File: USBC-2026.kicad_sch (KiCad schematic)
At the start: 28 parts, among them IC1 TPS25752ASRSMR, J1 USB_C_Receptacle, Q1 NMOS_Substrate, Q2 NMOS_Substrate, U1 TPS55288RPMR, U2 AT24C512C-SHM-B

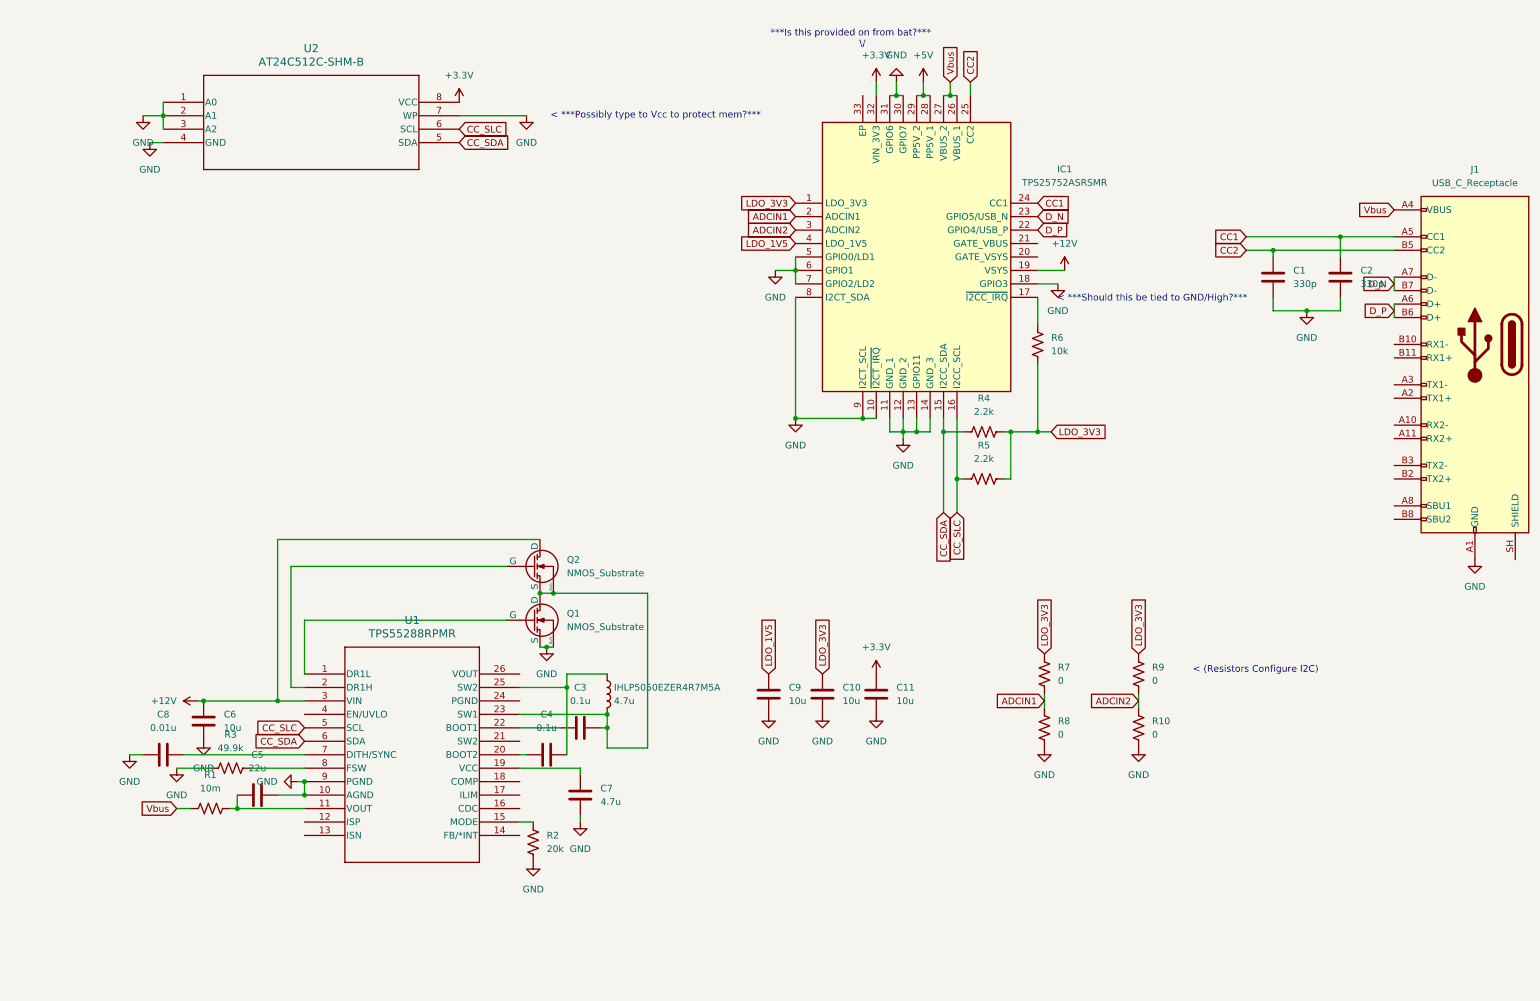
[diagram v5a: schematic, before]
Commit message: Grounded pins to select I2C address index 2.
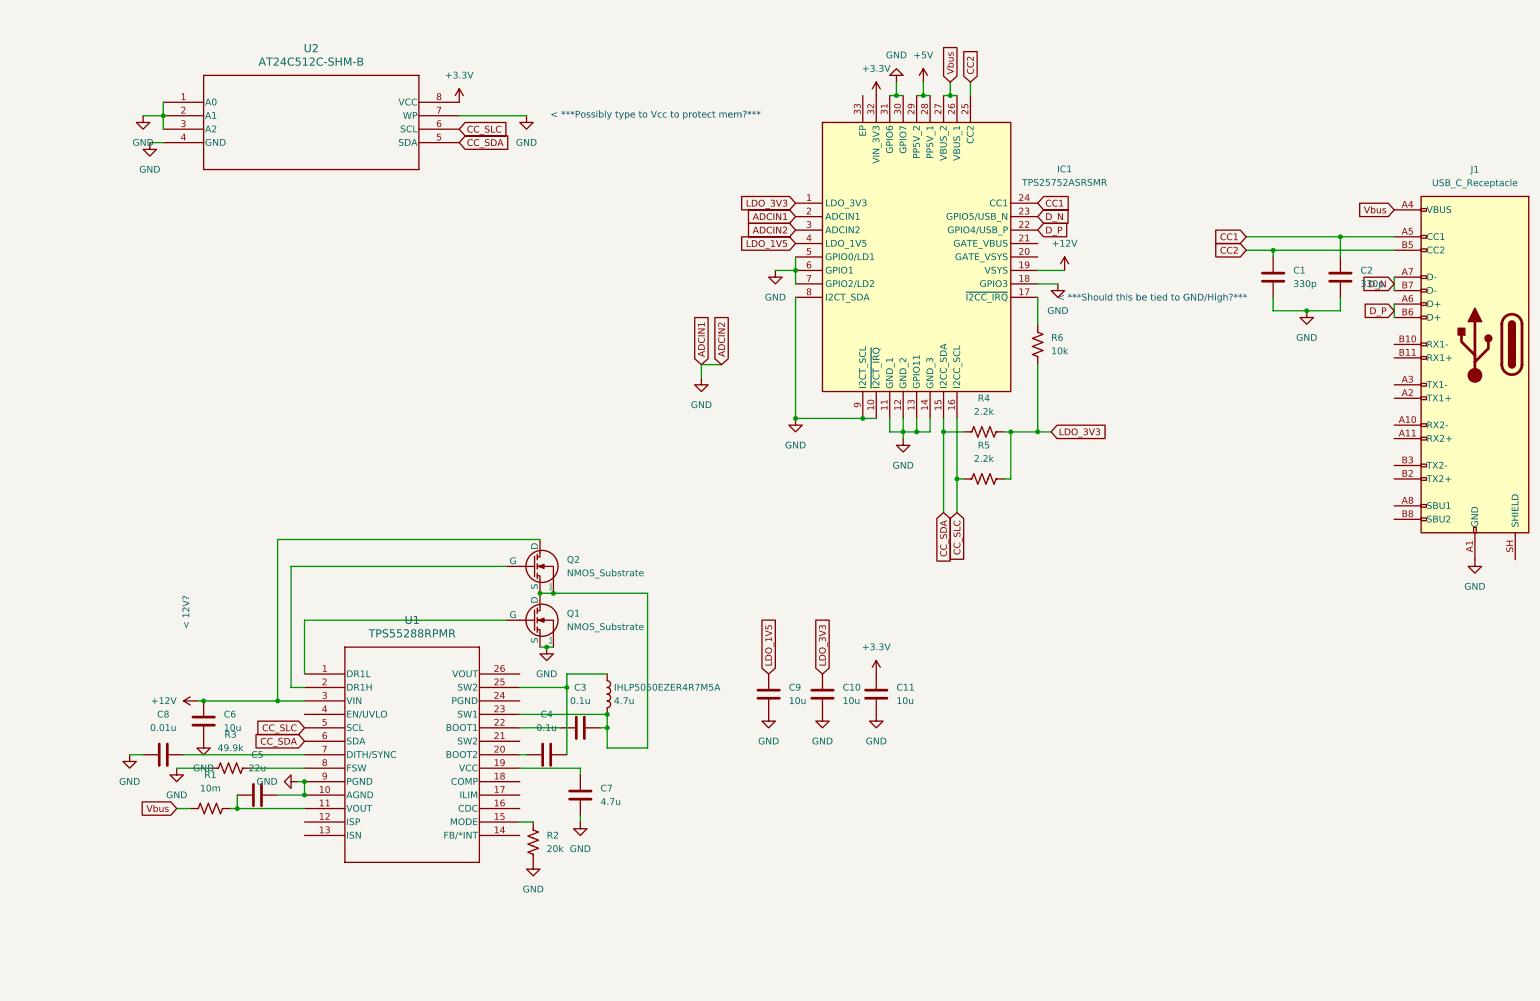
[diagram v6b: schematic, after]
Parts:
- removed R10, R7, R8, R9: 0, symbol Device:R_US
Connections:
- net ADCIN1 is gone; now on net GND: IC1.2 (ADCIN1)
- net ADCIN2 is gone; now on net GND: IC1.3 (ADCIN2)
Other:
- note added: "< 12V?"
- note removed: "***Is this provided on from bat?*** \/"
- note removed: "< (Resistors Configure I2C)"

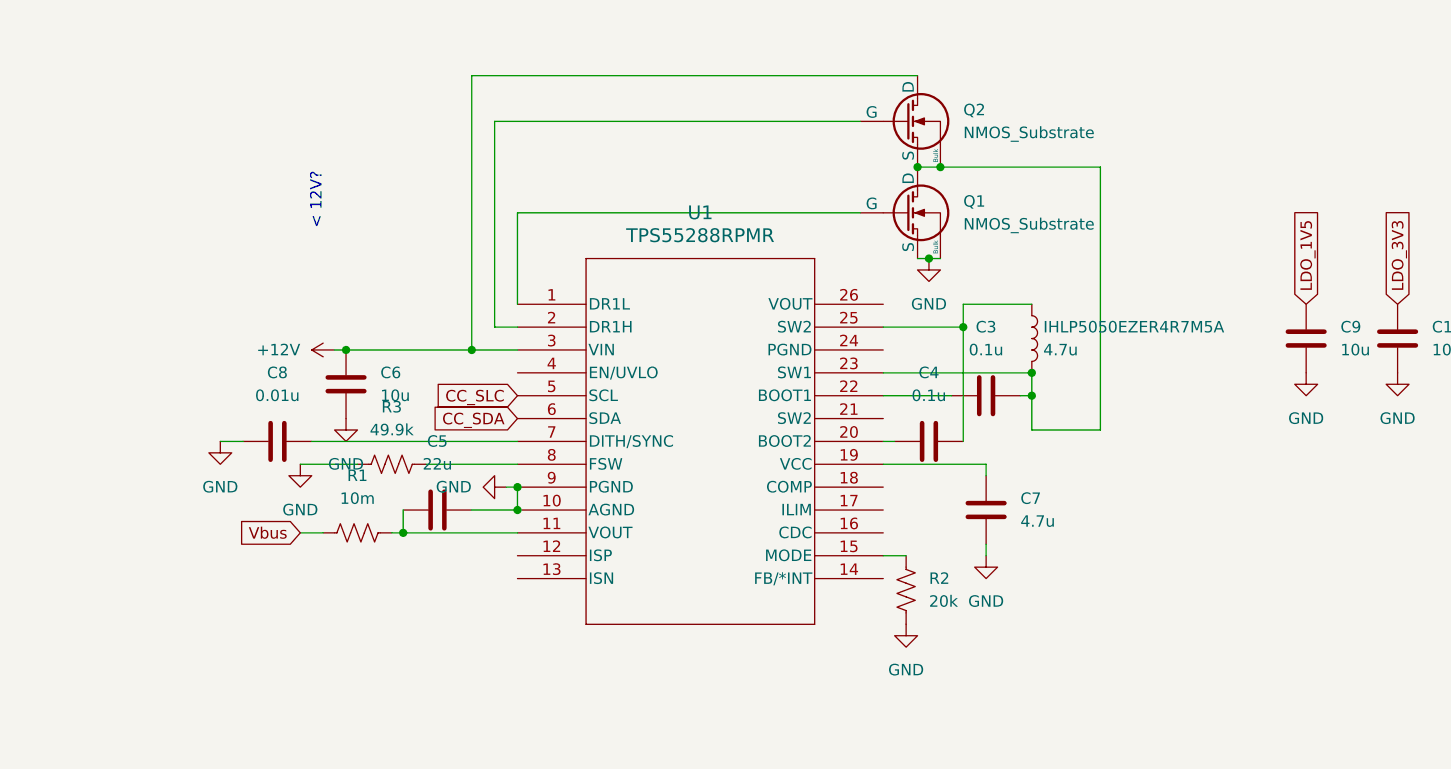
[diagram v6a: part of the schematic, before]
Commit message: Calculated and implemented loop stability components.
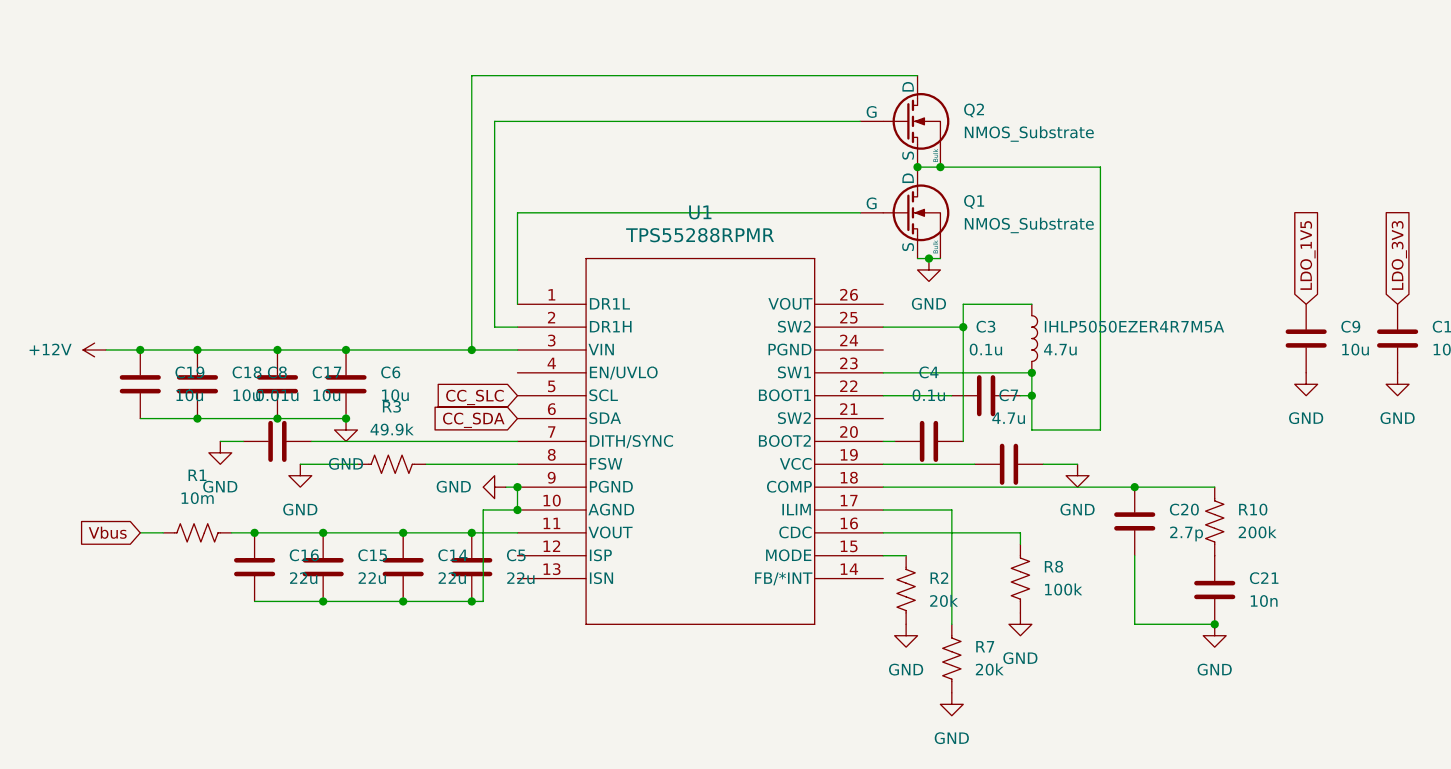
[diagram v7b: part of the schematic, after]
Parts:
- added C14, C15, C16: 22u, symbol Device:C
- added C17, C18, C19: 10u, symbol Device:C
- added C20: 2.7p, symbol Device:C
- added C21: 10n, symbol Device:C
- added R10: 200k, symbol Device:R_US
- added R7: 20k, symbol Device:R_US
- added R8: 100k, symbol Device:R_US
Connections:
- net +12V: now also C17.1, C18.1, C19.1
- net GND: now also C5.2, C7.2, C14.2, C15.2, C16.2, C17.2, C18.2, C19.2, C20.1, C21.1, R7.1, R8.1; no longer C5.1, C7.1
- net at R1.2, U1.11 (VOUT): now also C5.1, C14.1, C15.1, C16.1; no longer C5.2
- net at U1.19 (VCC): now also C7.1; no longer C7.2
- net at U1.16 (CDC): now also R8.2
- net at U1.17 (ILIM): now also R7.2
- net at U1.18 (COMP): now also C20.2, R10.2
- new net: C21.2, R10.1
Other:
- note removed: "< 12V?"
- moved on the sheet: C7, R1

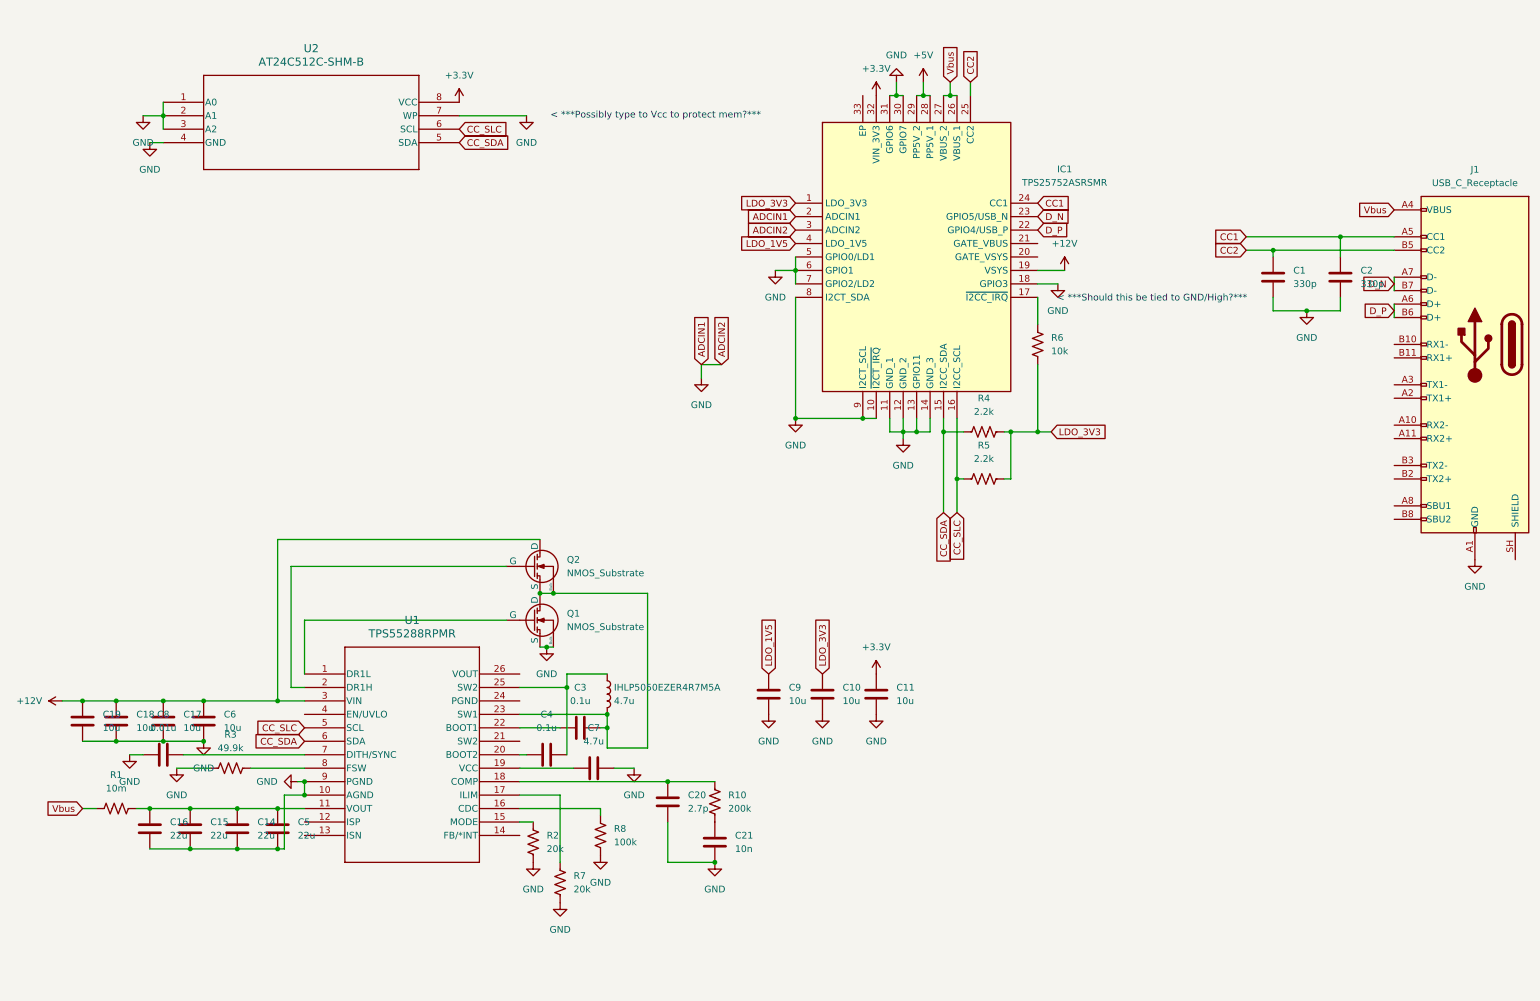
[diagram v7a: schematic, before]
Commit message: Added specific NMOS IC and split into subsheets.
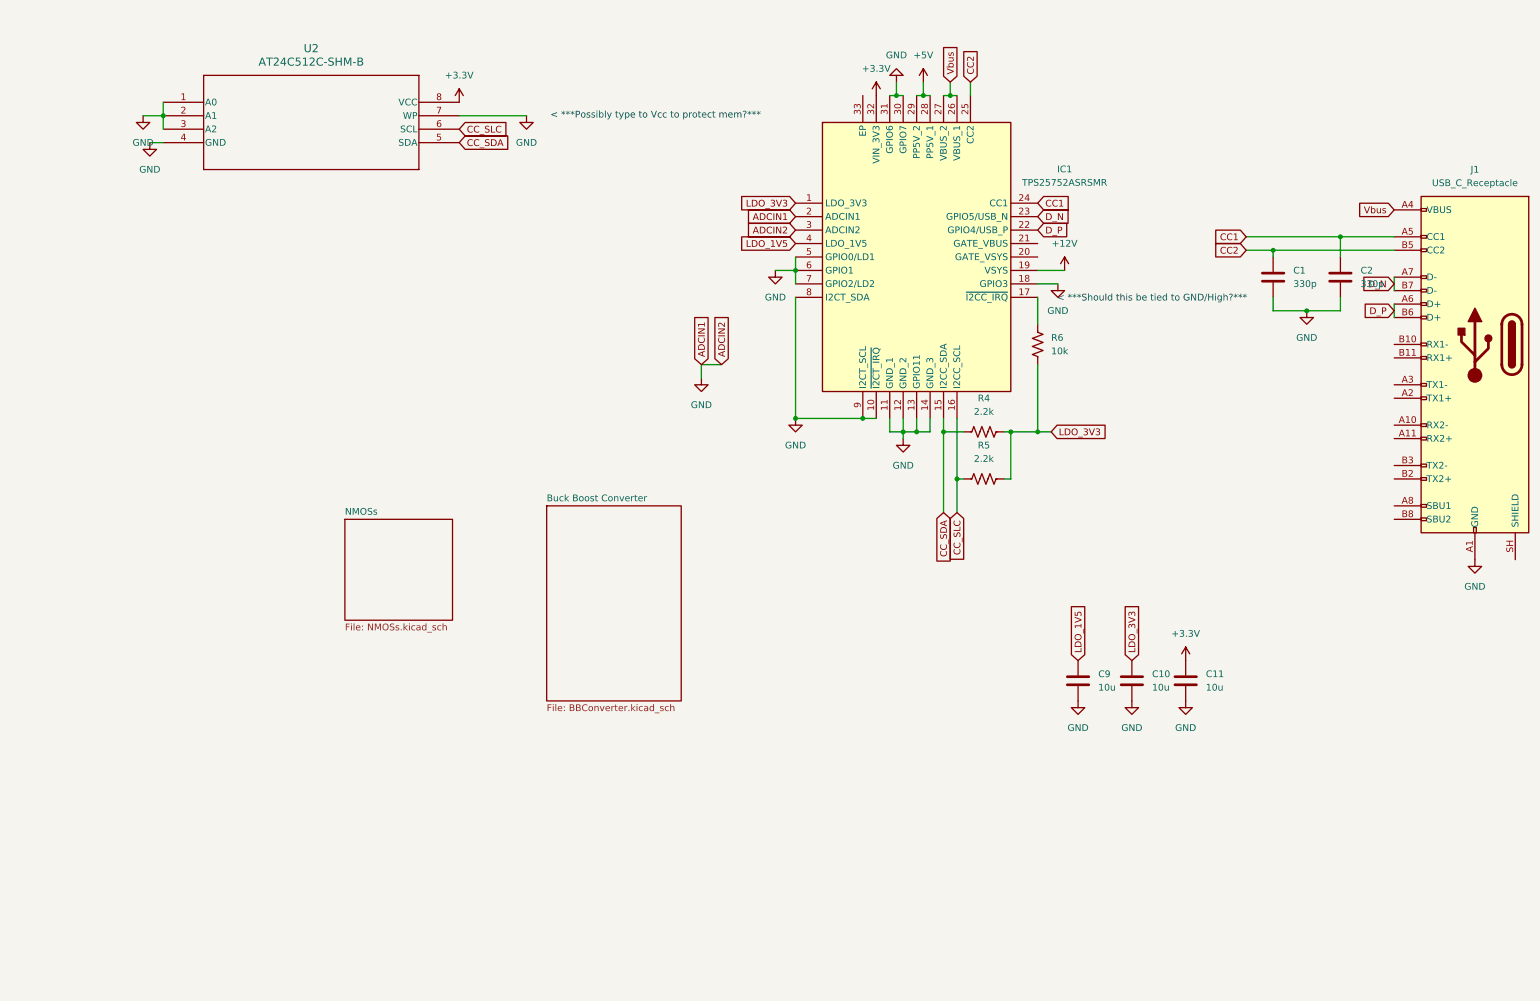
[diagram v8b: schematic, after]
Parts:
- removed C14, C15, C16, C5: 22u, symbol Device:C
- removed C17, C18, C19, C6: 10u, symbol Device:C
- removed C20: 2.7p, symbol Device:C
- removed C21: 10n, symbol Device:C
- removed C3, C4: 0.1u, symbol Device:C
- removed C7: 4.7u, symbol Device:C
- removed C8: 0.01u, symbol Device:C
- removed IHLP5050EZER4R7M5A: 4.7u, symbol Device:L
- removed Q1, Q2: NMOS_Substrate, symbol Simulation_SPICE:NMOS_Substrate
- removed R1: 10m, symbol Device:R_US
- removed R10: 200k, symbol Device:R_US
- removed R2, R7: 20k, symbol Device:R_US
- removed R3: 49.9k, symbol Device:R_US
- removed R8: 100k, symbol Device:R_US
- removed U1: TPS55288RPMR, VQFN-HR26_RPM_TEX, symbol symbol_library:TPS55288RPMR
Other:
- added sheet Buck Boost Converter (BBConverter.kicad_sch)
- added sheet NMOSs (NMOSs.kicad_sch)
- moved on the sheet: C10, C11, C9
